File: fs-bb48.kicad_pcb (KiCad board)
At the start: 2 copper layers, 35 x 12.1 mm, 17 parts, among them P1 USB, P2 SWD, P3 PWR, P4 EXT, T1 TOUCH_PAD, U1 MKL27Z256VFM4, U2 EMIF02-USB03F2

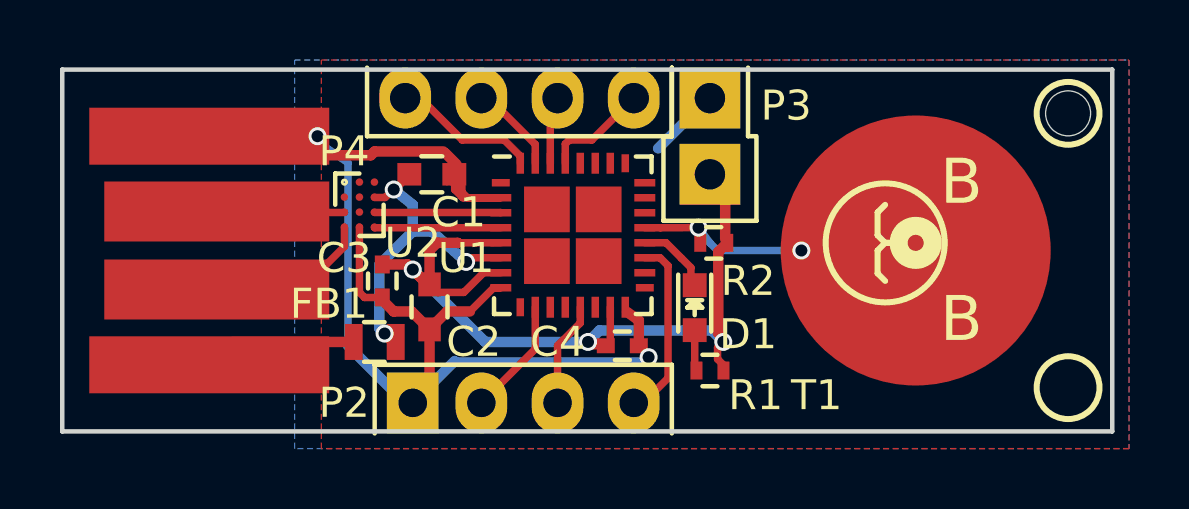
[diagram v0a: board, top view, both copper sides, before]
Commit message: finish BBB
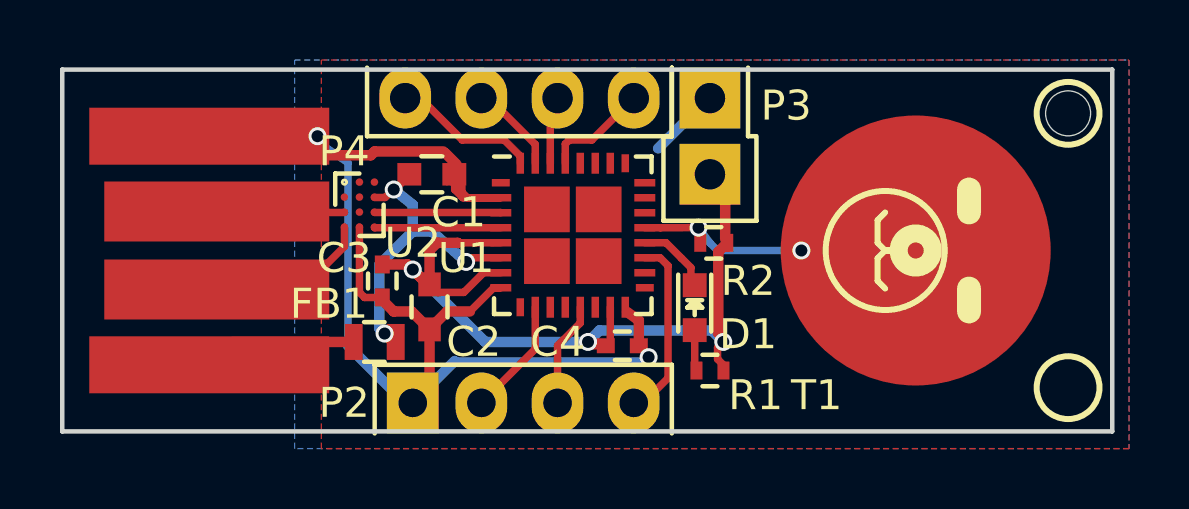
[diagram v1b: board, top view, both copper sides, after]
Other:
- board text removed: "B"
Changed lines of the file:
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@@
   (layers
     (0 F.Cu signal)
-    (31 B.Cu signal hide)
+    (31 B.Cu signal)
     (32 B.Adhes user)
     (33 F.Adhes user)
-    (34 B.Paste user hide)
+    (34 B.Paste user)
     (35 F.Paste user)
-    (36 B.SilkS user hide)
+    (36 B.SilkS user)
     (37 F.SilkS user)
-    (38 B.Mask user hide)
+    (38 B.Mask user)
     (39 F.Mask user)
     (40 Dwgs.User user)
@@
     (47 F.CrtYd user hide)
     (48 B.Fab user hide)
-    (49 F.Fab user)
+    (49 F.Fab user hide)
   )
   (setup
@@
     (pad_to_mask_clearance 0.2)
     (solder_mask_min_width 0.1)
-    (aux_axis_origin 154.94 106.68)
-    (grid_origin 154.94 106.68)
-    (visible_elements 7FFFFBB7)
+    (aux_axis_origin 154.94 106.934)
+    (grid_origin 154.94 106.934)
+    (visible_elements 7FFFFFFF)
     (pcbplotparams
       (layerselection 0x010fc_80000001)
@@
       (solder_mask_margin 0.13) (solder_paste_margin 0.025) (clearance 0.05))
   )
-  (gr_circle (center 154.94 106.68) (end 155.194 107.188) (layer F.SilkS) (width 0.6))
-  (gr_line (start 153.67 107.696) (end 153.924 107.95) (angle 90) (layer F.SilkS) (width 0.2))
-  (gr_line (start 153.67 106.934) (end 153.67 107.696) (angle 90) (layer F.SilkS) (width 0.2))
-  (gr_line (start 153.924 106.68) (end 153.67 106.934) (angle 90) (layer F.SilkS) (width 0.2))
-  (gr_line (start 154.178 106.68) (end 153.924 106.68) (angle 90) (layer F.SilkS) (width 0.2))
-  (gr_line (start 153.67 105.664) (end 153.924 105.41) (angle 90) (layer F.SilkS) (width 0.2))
-  (gr_line (start 153.67 106.426) (end 153.67 105.664) (angle 90) (layer F.SilkS) (width 0.2))
-  (gr_line (start 153.924 106.68) (end 153.67 106.426) (angle 90) (layer F.SilkS) (width 0.2))
-  (gr_line (start 154.178 106.68) (end 153.924 106.68) (angle 90) (layer F.SilkS) (width 0.2))
-  (gr_text B (at 156.464 109.22) (layer F.SilkS)
-    (effects (font (size 1.5 1.5) (thickness 0.3)))
-  )
-  (gr_text B (at 156.464 104.648) (layer F.SilkS)
-    (effects (font (size 1.5 1.5) (thickness 0.3)))
-  )
-  (gr_circle (center 153.924 106.68) (end 155.194 108.204) (layer F.SilkS) (width 0.2))
+  (gr_line (start 156.718 108.204) (end 156.718 108.966) (angle 90) (layer F.SilkS) (width 0.8))
+  (gr_line (start 156.718 104.902) (end 156.718 105.664) (angle 90) (layer F.SilkS) (width 0.8))
+  (gr_circle (center 154.94 106.934) (end 155.194 107.442) (layer F.SilkS) (width 0.6))
+  (gr_line (start 153.67 107.95) (end 153.924 108.204) (angle 90) (layer F.SilkS) (width 0.2))
+  (gr_line (start 153.67 107.188) (end 153.67 107.95) (angle 90) (layer F.SilkS) (width 0.2))
+  (gr_line (start 153.924 106.934) (end 153.67 107.188) (angle 90) (layer F.SilkS) (width 0.2))
+  (gr_line (start 154.178 106.934) (end 153.924 106.934) (angle 90) (layer F.SilkS) (width 0.2))
+  (gr_line (start 153.67 105.918) (end 153.924 105.664) (angle 90) (layer F.SilkS) (width 0.2))
+  (gr_line (start 153.67 106.68) (end 153.67 105.918) (angle 90) (layer F.SilkS) (width 0.2))
+  (gr_line (start 153.924 106.934) (end 153.67 106.68) (angle 90) (layer F.SilkS) (width 0.2))
+  (gr_line (start 154.178 106.934) (end 153.924 106.934) (angle 90) (layer F.SilkS) (width 0.2))
+  (gr_circle (center 153.924 106.934) (end 155.194 108.458) (layer F.SilkS) (width 0.2))
   (gr_text FS-BB48 (at 154.178 102.87) (layer B.SilkS)
     (effects (font (size 1.2 1.2) (thickness 0.3) italic) (justify mirror))

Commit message: Added CE marking
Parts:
- added CE: CE_5mm, Symbols:Symbol_CE_SilkScreen_5mm, B.Cu at (142.7, 105.9)
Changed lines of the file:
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@@
     (tracks 190)
     (zones 0)
-    (modules 17)
+    (modules 18)
     (nets 20)
   )
   (page A4)
   (layers
-    (0 F.Cu signal)
+    (0 F.Cu signal hide)
     (31 B.Cu signal)
     (32 B.Adhes user)
@@
     (35 F.Paste user)
     (36 B.SilkS user)
-    (37 F.SilkS user)
+    (37 F.SilkS user hide)
     (38 B.Mask user)
     (39 F.Mask user)
@@
     (aux_axis_origin 154.94 106.934)
     (grid_origin 154.94 106.934)
-    (visible_elements 7FFFFFFF)
+    (visible_elements 7FFFFDFF)
     (pcbplotparams
       (layerselection 0x010fc_80000001)
@@
   (module fs-bb48:Hole (layer F.Cu)
     (at 160.02 102.362)
-    (fp_text reference H1 (at 2.54 1.524) (layer F.SilkS) hide
-      (effects (font (size 1 1) (thickness 0.15)))
-    )
-    (fp_text value 2mm (at 2.032 -1.27) (layer F.Fab) hide
+    (fp_text reference H1 (at 3.302 0) (layer F.SilkS) hide
+      (effects (font (size 1 1) (thickness 0.15)))
+    )
+    (fp_text value 2mm (at 2.286 -2.54) (layer F.Fab) hide
       (effects (font (size 1 1) (thickness 0.15)))
     )
@@
       (solder_mask_margin 0.13) (solder_paste_margin 0.025) (clearance 0.05))
   )
+  (module Symbols:Symbol_CE_SilkScreen_5mm (layer B.Cu)
+    (at 142.748 105.918 180)
+    (fp_text reference CE (at -1.016 8.89 180) (layer B.Fab) hide
+      (effects (font (size 1 1) (thickness 0.15)) (justify mirror))
+    )
+    (fp_text value CE_5mm (at -0.254 11.176 180) (layer B.Fab) hide
+      (effects (font (size 1 1) (thickness 0.15)) (justify mirror))
+    )
+    (fp_line (start 3.1875 -1.875) (end 3.3125 -1.875) (layer B.SilkS) (width 0.25))
+    (fp_line (start 3.3125 -1.875) (end 3.3125 -2.375) (layer B.SilkS) (width 0.25))
+    (fp_line (start 3.3125 -2.375) (end 3.1875 -2.375) (layer B.SilkS) (width 0.25))
+    (fp_line (start 3.1875 2.375) (end 3.3125 2.375) (layer B.SilkS) (width 0.25))
+    (fp_line (start 3.3125 2.375) (end 3.3125 1.875) (layer B.SilkS) (width 0.25))
+    (fp_line (start 3.3125 1.875) (end 3.1875 1.875) (layer B.SilkS) (width 0.25))
+    (fp_line (start 2.5625 -0.25) (end 2.6875 -0.25) (layer B.SilkS) (width 0.25))
+    (fp_line (start 2.6875 0.25) (end 2.5625 0.25) (layer B.SilkS) (width 0.25))
+    (fp_line (start 2.6875 0.25) (end 2.8125 0.25) (layer B.SilkS) (width 0.25))
+    (fp_line (start 2.8125 0.25) (end 2.8125 -0.25) (layer B.SilkS) (width 0.25))
+    (fp_line (start 2.8125 -0.25) (end 2.6875 -0.25) (layer B.SilkS) (width 0.25))
+    (fp_line (start -1.0625 -1.875) (end -0.9375 -1.875) (layer B.SilkS) (width 0.25))
+    (fp_line (start -0.9375 -1.875) (end -0.9375 -2.375) (layer B.SilkS) (width 0.25))
+    (fp_line (start -0.9375 -2.375) (end -1.0625 -2.375) (layer B.SilkS) (width 0.25))
+    (fp_line (start -0.9375 2.375) (end -1.0625 2.375) (layer B.SilkS) (width 0.25))
+    (fp_line (start -0.9375 2.375) (end -0.9375 1.875) (layer B.SilkS) (width 0.25))
+    (fp_line (start -0.9375 1.875) (end -1.0625 1.875) (layer B.SilkS) (width 0.25))
+    (fp_arc (start -1.0625 0) (end -1.431502 -2.092716) (angle -160) (layer B.SilkS) (width 0.75))
+    (fp_arc (start -1.0625 0) (end -1.0625 -2.375) (angle -180) (layer B.SilkS) (width 0.25))
+    (fp_arc (start -1.0625 0) (end -1.0625 -1.875) (angle -180) (layer B.SilkS) (width 0.25))
+    (fp_line (start -1.0625 2.375) (end -1.0625 1.875) (layer B.SilkS) (width 0.25))
+    (fp_line (start -1.0625 -1.875) (end -1.0625 -2.375) (layer B.SilkS) (width 0.25))
+    (fp_line (start 3.1875 -1.875) (end 3.1875 -2.375) (layer B.SilkS) (width 0.25))
+    (fp_line (start 3.1875 2.375) (end 3.1875 1.875) (layer B.SilkS) (width 0.25))
+    (fp_arc (start 3.1875 0) (end 3.1875 -1.875) (angle -180) (layer B.SilkS) (width 0.25))
+    (fp_arc (start 3.1875 0) (end 3.1875 -2.375) (angle -180) (layer B.SilkS) (width 0.25))
+    (fp_line (start 2.5625 0) (end 1.0625 0) (layer B.SilkS) (width 0.75))
+    (fp_arc (start 3.1875 0) (end 2.818498 -2.092716) (angle -160) (layer B.SilkS) (width 0.75))
+  )
   (gr_line (start 156.718 108.204) (end 156.718 108.966) (angle 90) (layer F.SilkS) (width 0.8))

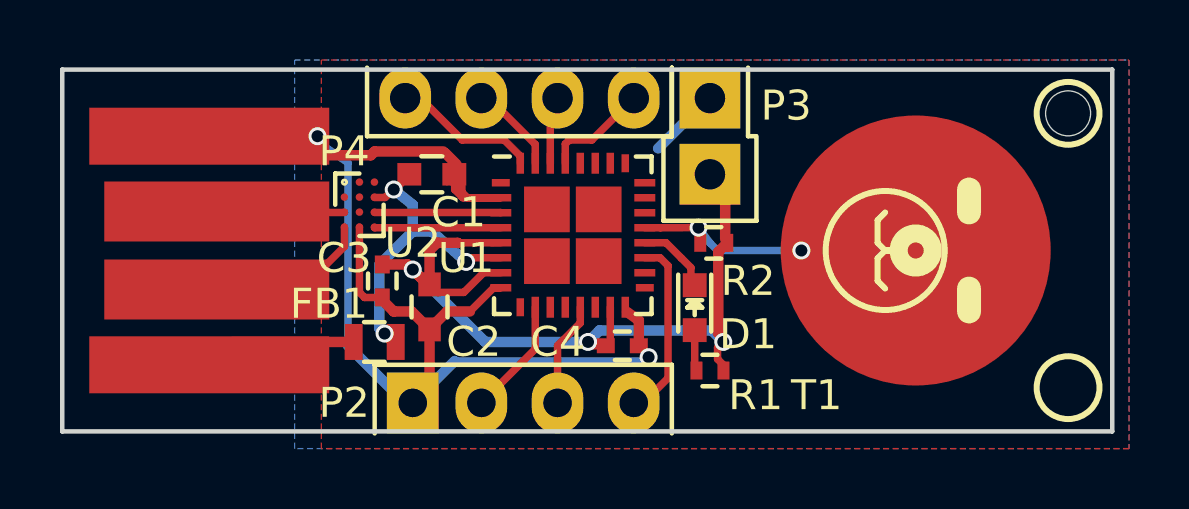
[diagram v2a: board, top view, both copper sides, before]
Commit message: move silks
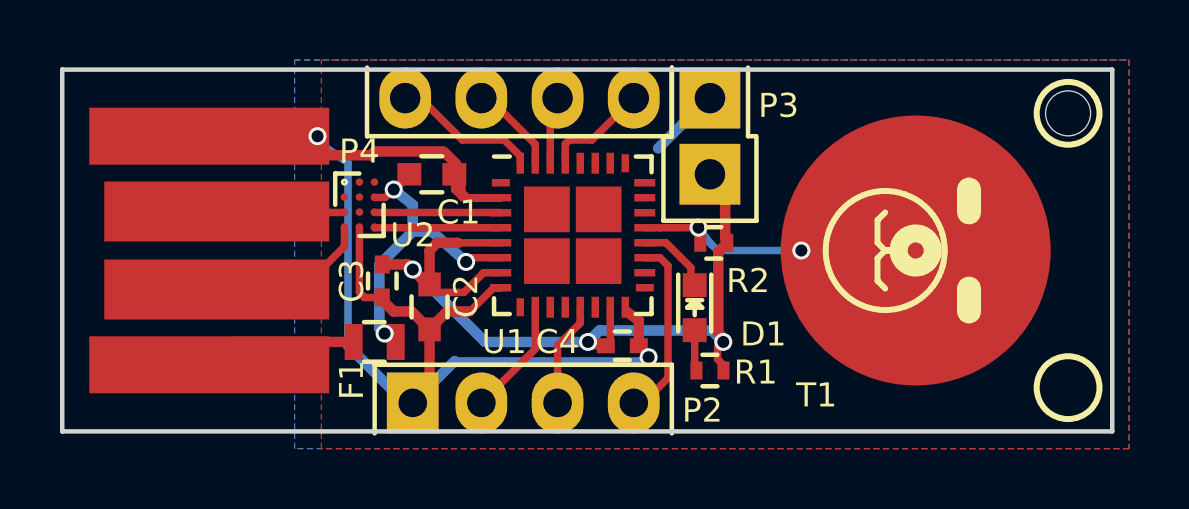
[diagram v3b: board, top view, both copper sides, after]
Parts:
- renumbered FB1 to F1
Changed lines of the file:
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@@
     (links 37)
     (no_connects 0)
-    (area 122.827 95.395 164.390619 116.799)
+    (area 122.827 93.617 164.597 116.799)
     (thickness 2)
     (drawings 20)
@@
   (page A4)
   (layers
-    (0 F.Cu signal hide)
-    (31 B.Cu signal)
+    (0 F.Cu signal)
+    (31 B.Cu signal hide)
     (32 B.Adhes user)
     (33 F.Adhes user)
     (34 B.Paste user)
     (35 F.Paste user)
-    (36 B.SilkS user)
-    (37 F.SilkS user hide)
-    (38 B.Mask user)
+    (36 B.SilkS user hide)
+    (37 F.SilkS user)
+    (38 B.Mask user hide)
     (39 F.Mask user)
     (40 Dwgs.User user)
@@
     (aux_axis_origin 154.94 106.934)
     (grid_origin 154.94 106.934)
-    (visible_elements 7FFFFDFF)
+    (visible_elements 7FFFFBBF)
     (pcbplotparams
       (layerselection 0x010fc_80000001)
@@
       (plotinvisibletext false)
       (padsonsilk false)
-      (subtractmaskfromsilk false)
+      (subtractmaskfromsilk true)
       (outputformat 1)
       (mirror false)
@@
     (descr "Through hole pin header")
     (tags "pin header")
-    (fp_text reference P2 (at 0 9.652 360) (layer F.SilkS)
-      (effects (font (size 1 1) (thickness 0.15)))
+    (fp_text reference P2 (at 0.254 -2.286 540) (layer F.SilkS)
+      (effects (font (size 0.8 0.8) (thickness 0.15)))
     )
     (fp_text value SWD (at 3.81 6.096 360) (layer F.Fab)
@@
     (tags "Neosid, Inductor, SM0603CG, Festinduktivitaet, SMD,")
     (attr smd)
-    (fp_text reference FB1 (at -1.524 -1.27) (layer F.SilkS)
-      (effects (font (size 1 1) (thickness 0.15)))
+    (fp_text reference F1 (at -0.762 1.27 90) (layer F.SilkS)
+      (effects (font (size 0.8 0.8) (thickness 0.15)))
     )
     (fp_text value 330ohm (at -0.762 4.318) (layer F.Fab)
@@
     (attr smd)
     (fp_text reference C4 (at -2.159 -0.127) (layer F.SilkS)
-      (effects (font (size 1 1) (thickness 0.15)))
+      (effects (font (size 0.8 0.8) (thickness 0.15)))
     )
     (fp_text value 0.1uF (at -0.381 5.715) (layer F.Fab)
@@
     (at 154.94 106.934 270)
     (fp_text reference T1 (at 4.826 3.302 360) (layer F.SilkS)
-      (effects (font (size 1 1) (thickness 0.15)))
+      (effects (font (size 0.8 0.8) (thickness 0.15)))
     )
     (fp_text value TOUCH_PAD (at -7.874 0 360) (layer F.Fab)
@@
     (attr smd)
     (fp_text reference C1 (at 0.889 1.27) (layer F.SilkS)
-      (effects (font (size 1 1) (thickness 0.15)))
+      (effects (font (size 0.8 0.8) (thickness 0.15)))
     )
     (fp_text value 2.2uF (at 0.889 -7.874) (layer F.Fab)
@@
     (tags "capacitor 0402")
     (attr smd)
-    (fp_text reference C3 (at -0.762 1.27 360) (layer F.SilkS)
-      (effects (font (size 1 1) (thickness 0.15)))
+    (fp_text reference C3 (at 0 1.016 450) (layer F.SilkS)
+      (effects (font (size 0.8 0.8) (thickness 0.15)))
     )
     (fp_text value 0.1uF (at 0 13.208 270) (layer F.Fab)
@@
     (tags "capacitor 0603")
     (attr smd)
-    (fp_text reference C2 (at 1.1684 -1.4732 360) (layer F.SilkS)
-      (effects (font (size 1 1) (thickness 0.15)))
+    (fp_text reference C2 (at -0.3556 -1.2192 450) (layer F.SilkS)
+      (effects (font (size 0.8 0.8) (thickness 0.15)))
     )
     (fp_text value 2.2uF (at 2.1844 13.0048 270) (layer F.Fab)
@@
     (attr smd)
     (fp_text reference R2 (at -1.143 -1.27 180) (layer F.SilkS)
-      (effects (font (size 1 1) (thickness 0.15)))
+      (effects (font (size 0.8 0.8) (thickness 0.15)))
     )
     (fp_text value 1M (at -14.859 0 180) (layer F.Fab)
@@
     (tags "resistor 0402")
     (attr smd)
-    (fp_text reference R1 (at 1.524 0.8255) (layer F.SilkS)
-      (effects (font (size 1 1) (thickness 0.15)))
+    (fp_text reference R1 (at 1.524 0.0635) (layer F.SilkS)
+      (effects (font (size 0.8 0.8) (thickness 0.15)))
     )
     (fp_text value 510R (at 2.54 4.8895) (layer F.Fab)
@@
     (tags "LED led 0603 SMD smd SMT smt smdled SMDLED smtled SMTLED")
     (attr smd)
-    (fp_text reference D1 (at 0.889 -1.778 360) (layer F.SilkS)
-      (effects (font (size 1 1) (thickness 0.15)))
+    (fp_text reference D1 (at 0.889 -2.286 360) (layer F.SilkS)
+      (effects (font (size 0.8 0.8) (thickness 0.15)))
     )
     (fp_text value LED (at 0.381 -15.494 270) (layer F.Fab)
@@
     (descr "Through hole pin header")
     (tags "pin header")
-    (fp_text reference P3 (at -2.54 2.286 180) (layer F.SilkS)
-      (effects (font (size 1 1) (thickness 0.15)))
+    (fp_text reference P3 (at -2.286 2.286 180) (layer F.SilkS)
+      (effects (font (size 0.8 0.8) (thickness 0.15)))
     )
     (fp_text value PWR (at -0.508 7.874 180) (layer F.Fab)
@@
     (descr "Through hole pin header")
     (tags "pin header")
-    (fp_text reference P4 (at 1.778 9.652 360) (layer F.SilkS)
-      (effects (font (size 1 1) (thickness 0.15)))
+    (fp_text reference P4 (at 1.778 9.144 360) (layer F.SilkS)
+      (effects (font (size 0.8 0.8) (thickness 0.15)))
     )
     (fp_text value EXT (at -2.794 0.762 360) (layer F.Fab)
@@
     (tags "QFN 0.5")
     (attr smd)
-    (fp_text reference U1 (at -3.556 0.762) (layer F.SilkS)
-      (effects (font (size 1 1) (thickness 0.15)))
+    (fp_text reference U1 (at -2.286 3.556) (layer F.SilkS)
+      (effects (font (size 0.8 0.8) (thickness 0.15)))
     )
     (fp_text value MKL27Z256VFM4 (at 2.54 7.874) (layer F.Fab)
@@
   (module fs-bb48:BGA-11 (layer F.Cu)
     (at 136.398 105.41)
-    (fp_text reference U2 (at 1.778 1.27) (layer F.SilkS)
-      (effects (font (size 1 1) (thickness 0.15)))
+    (fp_text reference U2 (at 1.778 1.016) (layer F.SilkS)
+      (effects (font (size 0.8 0.8) (thickness 0.15)))
     )
     (fp_text value EMIF02-USB03F2 (at 0 -6.35) (layer F.Fab)

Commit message: finish change of ESD chip
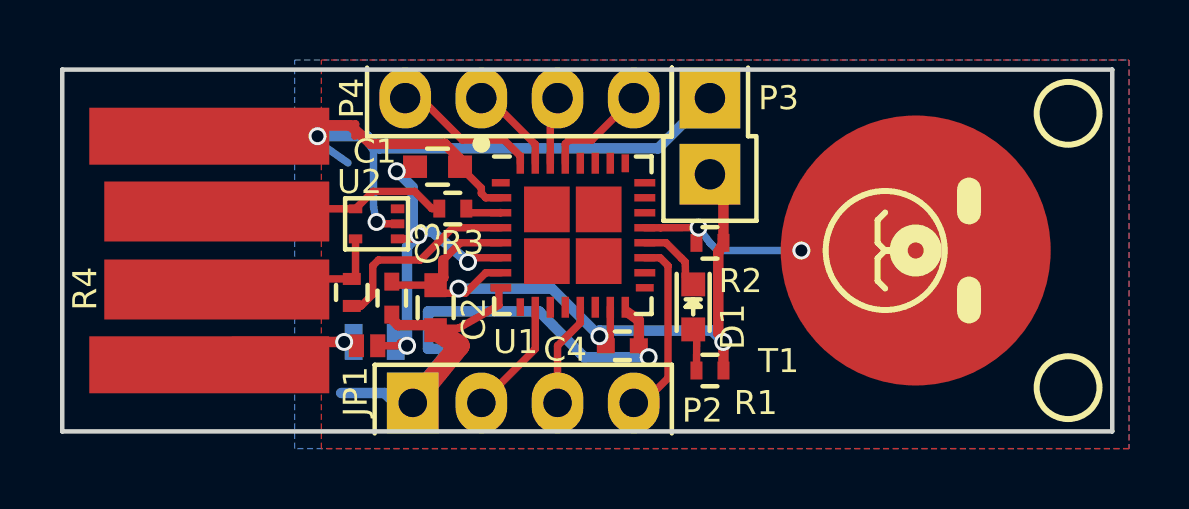
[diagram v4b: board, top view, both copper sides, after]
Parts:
- removed CE: CE_5mm, Symbols:Symbol_CE_SilkScreen_5mm
- removed F1: 330ohm, fs-bb48:Inductor_SM0603
- removed H1: 2mm, fs-bb48:Hole
- added CE1: CE_5mm, Symbols:Symbol_CE_SilkScreen_5mm, B.Cu at (130.2, 106.9)
- added FB1: 330ohm, fs-bb48:Inductor_SM0603, B.Cu at (136.9, 110.0)
- added JP1: Jumper_NC_Small, fs-bb48:SOLDER_JUMPER, F.Cu at (136.7, 110.1)
- added R3: 33R, fs-bb48:R_0402, F.Cu at (139.5, 105.5)
- added R4: 33R, fs-bb48:R_0402, F.Cu at (136.1, 108.3)
- C4: footprint Capacitors_SMD:C_0402 -> fs-bb48:C_0402
- U2: value EMIF02-USB03F2 -> NUP2114; footprint fs-bb48:BGA-11 -> fs-bb48:SOT-553
- moved FST-LOGO 14.4 mm to (144.7, 105.5)
- moved U2 0.85 mm to (137.0, 106.0), turned to 180 degrees
- moved C3 0.65 mm to (137.5, 108.5)
- moved C1 0.32 mm to (139.0, 104.1)
- moved C2 0.20 mm to (138.9, 108.8)
- moved R2 0.13 mm to (148.1, 106.7)
- moved D1 0.06 mm to (147.5, 108.8)
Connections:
- U1 pad 1: Net-(U1-Pad1) -> (no net)
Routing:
- net GND: track 56.4 -> 65.5 mm, vias 2 -> 3
- net /VBUS: track 11.0 -> 14.8 mm, vias 3 -> 4
- net /D+_: track 4.08 -> 7.93 mm
- net +3V3: track 32.8 -> 29.5 mm
- net /D+: track 4.22 -> 1.22 mm
- net /D-: track 4.22 -> 6.60 mm
- net /VBUS_: track 5.13 -> 5.70 mm, vias 0 -> 1
- net /D-_: track 5.49 -> 6.04 mm
